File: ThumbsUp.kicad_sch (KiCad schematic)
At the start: 56 parts, among them J1 52559-1233, J1L1 PJ-3200B, J1R1 PJ-3200B, J2 52559-1233, U1 ProMicro

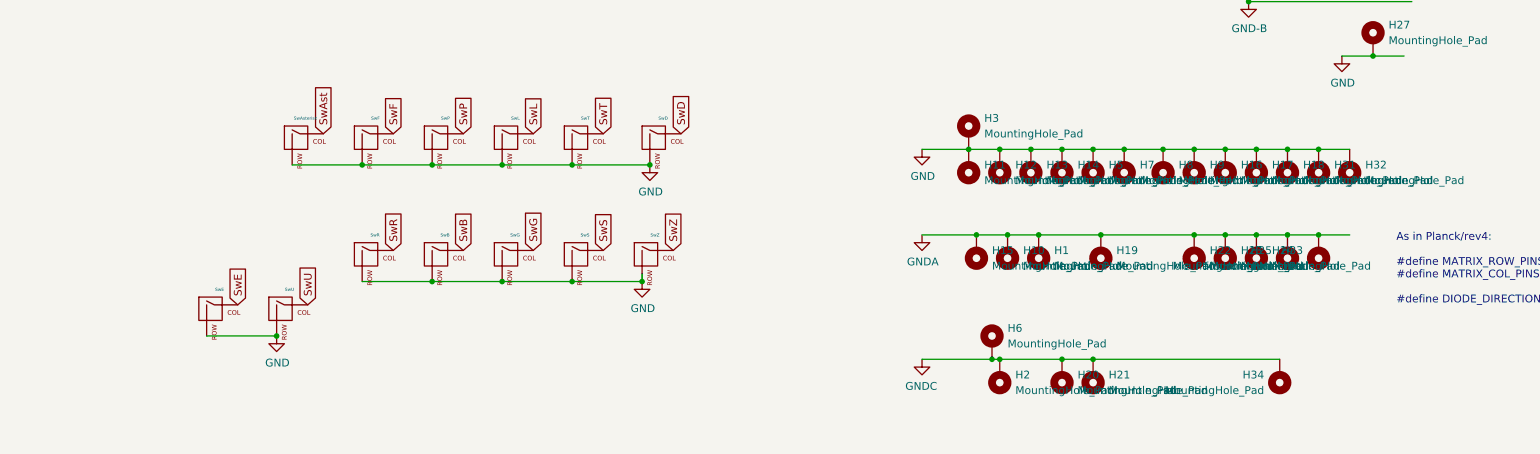
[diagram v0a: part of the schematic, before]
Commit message: v12: Branch: Made the thumb keys reversible - split their hinges, so they could be flipped over.
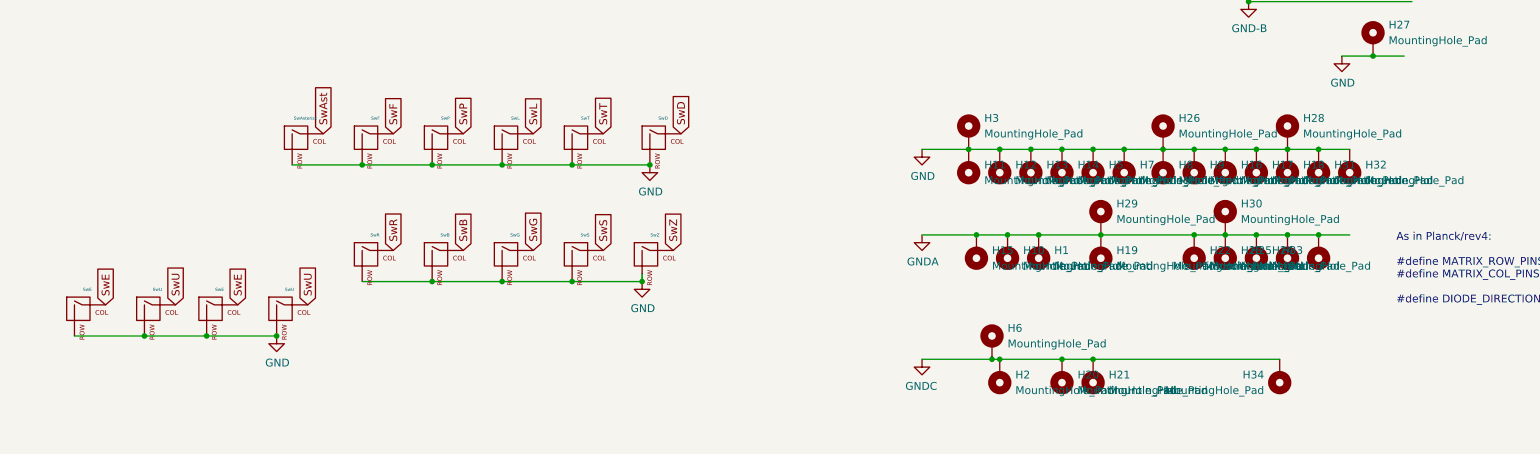
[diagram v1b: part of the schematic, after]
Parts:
- added H26, H28, H29, H30: MountingHole_Pad, MountingHole:MountingHole_3.5mm_Pad, symbol Mechanical:MountingHole_Pad
- added MX1: SwE, footprints:SW_D2FC_OMR, symbol ThumbsUp-rescue:MX-NoLED-MX_Alps_Hybrid
- added MX2: SwU, footprints:SW_D2FC_OMR, symbol ThumbsUp-rescue:MX-NoLED-MX_Alps_Hybrid
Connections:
- net GND: now also H26.1, H28.1, MX1.2 (ROW), MX2.2 (ROW)
- net GNDA: now also H29.1, H30.1
- net SwE: now also MX1.1 (COL)
- net SwU: now also MX2.1 (COL)
